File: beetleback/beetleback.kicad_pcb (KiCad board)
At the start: 4 copper layers, 20.8 x 28.3 mm, 23 parts, among them J1 Conn_01x05_Female, J3 motor_pad_1, J4 motor_pad_2, Q1 IRF7351TRPBF, Q2 IRF7351TRPBF, U1 ATtiny13A-SS, U2 DRV8701P

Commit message: Correct schematic booboo: use n-channel mosfets instead of a mixture
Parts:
- C1, C9: value 1uF 25V -> 1uF
- R3: value 33k TBC -> 220k
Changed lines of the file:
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@@
     (descr "Resistor SMD 0402 (1005 Metric), square (rectangular) end terminal, IPC_7351 nominal, (Body size source: IPC-SM-782 page 72, https://www.pcb-3d.com/wordpress/wp-content/uploads/ipc-sm-782a_amendment_1_and_2.pdf), generated with kicad-footprint-generator")
     (tags "resistor")
-    (property "LCSC" "C21190")
+    (property "LCSC" "C11702")
     (property "Sheet file" "beetleback.kicad_sch")
     (property "Sheet name" "")
@@
     (descr "Capacitor SMD 0402 (1005 Metric), square (rectangular) end terminal, IPC_7351 nominal, (Body size source: IPC-SM-782 page 76, https://www.pcb-3d.com/wordpress/wp-content/uploads/ipc-sm-782a_amendment_1_and_2.pdf), generated with kicad-footprint-generator")
     (tags "capacitor")
+    (property "LCSC" "C155422")
     (property "Sheet file" "beetleback.kicad_sch")
     (property "Sheet name" "")
@@
     (descr "Capacitor SMD 0402 (1005 Metric), square (rectangular) end terminal, IPC_7351 nominal, (Body size source: IPC-SM-782 page 76, https://www.pcb-3d.com/wordpress/wp-content/uploads/ipc-sm-782a_amendment_1_and_2.pdf), generated with kicad-footprint-generator")
     (tags "capacitor")
+    (property "LCSC" "C52923")
     (property "Sheet file" "beetleback.kicad_sch")
     (property "Sheet name" "")
@@
     (descr "Resistor SMD 0402 (1005 Metric), square (rectangular) end terminal, IPC_7351 nominal, (Body size source: IPC-SM-782 page 72, https://www.pcb-3d.com/wordpress/wp-content/uploads/ipc-sm-782a_amendment_1_and_2.pdf), generated with kicad-footprint-generator")
     (tags "resistor")
+    (property "LCSC" "C25767")
     (property "Sheet file" "beetleback.kicad_sch")
     (property "Sheet name" "")
@@
       (effects (font (size 1 1) (thickness 0.15)))
     )
-    (fp_text value "33k TBC" (at 0 1.17) (layer "F.Fab")
+    (fp_text value "220k" (at 0 1.17) (layer "F.Fab")
       (effects (font (size 1 1) (thickness 0.15)))
     )
@@
     (descr "JST XH series connector, B5B-XH-AM, with boss (http://www.jst-mfg.com/product/pdf/eng/eXH.pdf), generated with kicad-footprint-generator")
     (tags "connector JST XH vertical boss")
+    (property "LCSC" "C161872")
     (property "Sheet file" "beetleback.kicad_sch")
     (property "Sheet name" "")
@@
     (descr "VQFN, 24 Pin (http://www.ti.com/lit/ds/symlink/msp430f1101a.pdf), generated with kicad-footprint-generator ipc_noLead_generator.py")
     (tags "VQFN NoLead")
+    (property "LCSC" "C114178")
     (property "Sheet file" "beetleback.kicad_sch")
     (property "Sheet name" "")
@@
     (descr "Capacitor SMD 0402 (1005 Metric), square (rectangular) end terminal, IPC_7351 nominal, (Body size source: IPC-SM-782 page 76, https://www.pcb-3d.com/wordpress/wp-content/uploads/ipc-sm-782a_amendment_1_and_2.pdf), generated with kicad-footprint-generator")
     (tags "capacitor")
+    (property "LCSC" "C52923")
     (property "Sheet file" "beetleback.kicad_sch")
     (property "Sheet name" "")
@@
       (effects (font (size 1 1) (thickness 0.15)))
     )
-    (fp_text value "1uF 25V" (at 0 1.16 90) (layer "F.Fab") hide
+    (fp_text value "1uF" (at 0 1.16 90) (layer "F.Fab") hide
       (effects (font (size 1 1) (thickness 0.15)))
     )
@@
     (descr "Capacitor SMD 0402 (1005 Metric), square (rectangular) end terminal, IPC_7351 nominal, (Body size source: IPC-SM-782 page 76, https://www.pcb-3d.com/wordpress/wp-content/uploads/ipc-sm-782a_amendment_1_and_2.pdf), generated with kicad-footprint-generator")
     (tags "capacitor")
+    (property "LCSC" "C52923")
     (property "Sheet file" "beetleback.kicad_sch")
     (property "Sheet name" "")
@@
     (descr "Capacitor SMD 0402 (1005 Metric), square (rectangular) end terminal, IPC_7351 nominal, (Body size source: IPC-SM-782 page 76, https://www.pcb-3d.com/wordpress/wp-content/uploads/ipc-sm-782a_amendment_1_and_2.pdf), generated with kicad-footprint-generator")
     (tags "capacitor")
+    (property "LCSC" "C155422")
     (property "Sheet file" "beetleback.kicad_sch")
     (property "Sheet name" "")
@@
     (descr "SOIC, 8 Pin (JEDEC MS-012AA, https://www.analog.com/media/en/package-pcb-resources/package/pkg_pdf/soic_narrow-r/r_8.pdf), generated with kicad-footprint-generator ipc_gullwing_generator.py")
     (tags "SOIC SO")
+    (property "LCSC" "C68403")
     (property "Sheet file" "beetleback.kicad_sch")
     (property "Sheet name" "")
@@
       (net 5 "/GH2") (pinfunction "G"))
     (pad "3" smd roundrect (at -2.475 0.635 225) (size 1.95 0.6) (layers "F.Cu" "F.Paste" "F.Mask") (roundrect_rratio 0.25)
-      (net 7 "GND") (pinfunction "1"))
+      (net 7 "GND") (pinfunction "S"))
     (pad "4" smd roundrect (at -2.475 1.905 225) (size 1.95 0.6) (layers "F.Cu" "F.Paste" "F.Mask") (roundrect_rratio 0.25)
       (net 8 "/GL2") (pinfunction "G"))
@@
       (effects (font (size 1 1) (thickness 0.15)))
     )
-    (fp_text value "1uF 25V" (at 0 1.16 90) (layer "F.Fab") hide
+    (fp_text value "1uF" (at 0 1.16 90) (layer "F.Fab") hide
       (effects (font (size 1 1) (thickness 0.15)))
     )
@@
     (descr "Resistor SMD 0402 (1005 Metric), square (rectangular) end terminal, IPC_7351 nominal, (Body size source: IPC-SM-782 page 72, https://www.pcb-3d.com/wordpress/wp-content/uploads/ipc-sm-782a_amendment_1_and_2.pdf), generated with kicad-footprint-generator")
     (tags "resistor")
+    (property "LCSC" "C11702")
     (property "Sheet file" "beetleback.kicad_sch")
     (property "Sheet name" "")
@@
     (descr "Resistor SMD 0402 (1005 Metric), square (rectangular) end terminal, IPC_7351 nominal, (Body size source: IPC-SM-782 page 72, https://www.pcb-3d.com/wordpress/wp-content/uploads/ipc-sm-782a_amendment_1_and_2.pdf), generated with kicad-footprint-generator")
     (tags "resistor")
-    (property "LCSC" "C21190")
+    (property "LCSC" "C11702")
     (property "Sheet file" "beetleback.kicad_sch")
     (property "Sheet name" "")
@@
     (descr "SOIC, 8 Pin (JEDEC MS-012AA, https://www.analog.com/media/en/package-pcb-resources/package/pkg_pdf/soic_narrow-r/r_8.pdf), generated with kicad-footprint-generator ipc_gullwing_generator.py")
     (tags "SOIC SO")
+    (property "LCSC" "C68403")
     (property "Sheet file" "beetleback.kicad_sch")
     (property "Sheet name" "")
@@
       (net 3 "/GH1") (pinfunction "G"))
     (pad "3" smd roundrect (at -2.475 0.635 315) (size 1.95 0.6) (layers "F.Cu" "F.Paste" "F.Mask") (roundrect_rratio 0.25)
-      (net 7 "GND") (pinfunction "1"))
+      (net 7 "GND") (pinfunction "S"))
     (pad "4" smd roundrect (at -2.475 1.905 315) (size 1.95 0.6) (layers "F.Cu" "F.Paste" "F.Mask") (roundrect_rratio 0.25)
       (net 4 "/GL1") (pinfunction "G"))

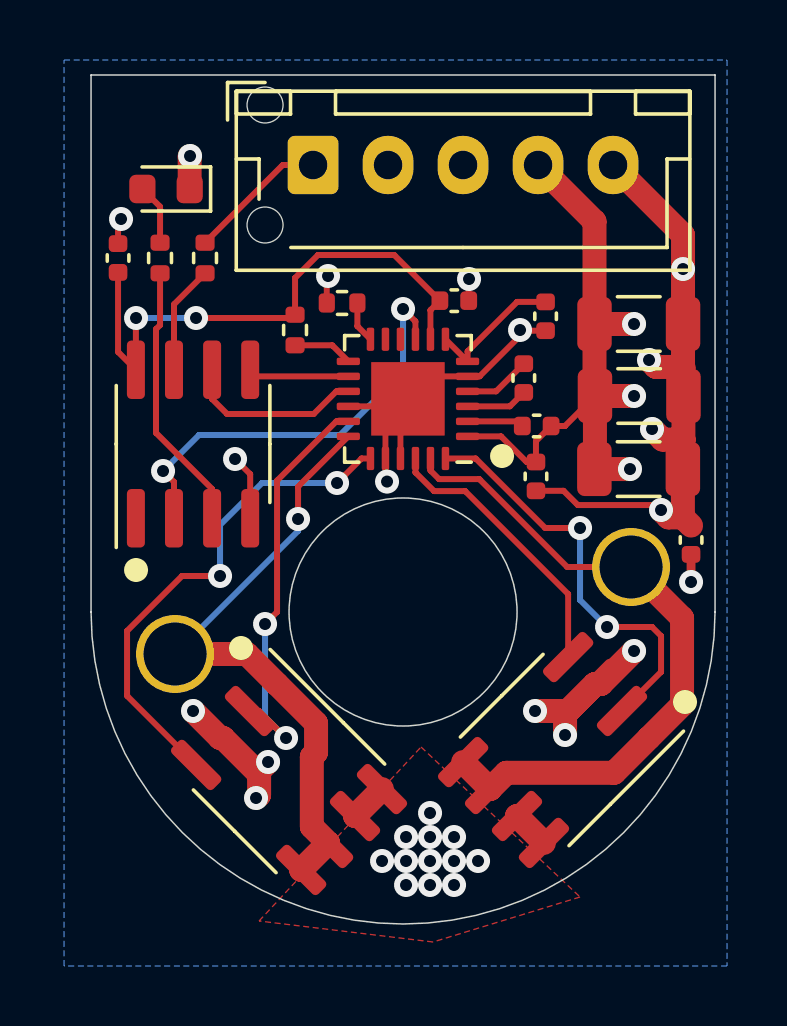
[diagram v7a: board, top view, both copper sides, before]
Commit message: more copper under fets, r3 dnp 0603
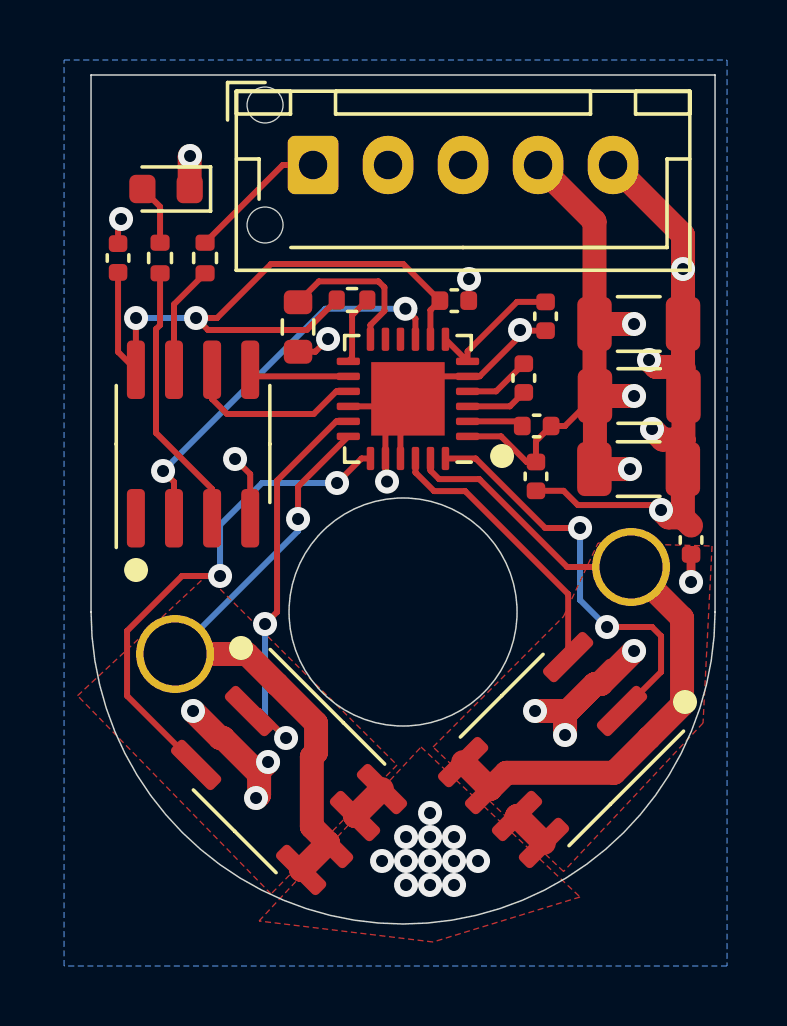
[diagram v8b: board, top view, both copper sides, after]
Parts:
- R3: value 220k -> DNP; footprint Resistor_SMD:R_0402_1005Metric -> Resistor_SMD:R_0603_1608Metric
- moved R2 2.15 mm to (148.3, 119.6), turned to 0 degrees
- moved R3 1.67 mm to (146.5, 120.5), turned to -90 degrees
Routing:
- net +3V3: track 19.0 -> 23.5 mm
- net Net-(R3-Pad1): track 1.39 -> 5.17 mm
- net /~FAULT: track 14.4 -> 13.2 mm
- added copper zone on F.Cu, net /MOTOR_PAD_1
- added copper zone on F.Cu, net /MOTOR_PAD_2
